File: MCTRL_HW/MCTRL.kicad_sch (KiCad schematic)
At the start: 22 parts, among them Q1 NMOS, Q2 NMOS, Q3 NMOS, Q4 NMOS, U1 IR2110, U2 IR2110

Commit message: more changes
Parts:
- removed Q1, Q2, Q3, Q4: NMOS, symbol Simulation_SPICE:NMOS
- added J1, J2, J3: 393570004, MCTRL:393570004, symbol MCTRL:393570004
- added U3, U4, U5, U6: IPD70R360P7SAUMA1, MCTRL:IPD70R360P7SAUMA1, symbol MCTRL:IPD70R360P7SAUMA1
- D1, D4: footprint (none) -> Diode_THT:D_DO-15_P12.70mm_Horizontal
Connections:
- net +3.3V: now also J2.1
- net +VDD: now also J1.1, U3.2 (DRAIN), U5.2 (DRAIN)
- net at D6.2 (A), R4.2: now also U6.1 (GATE)
- net at D2.2 (A), R1.2: now also U3.1 (GATE)
- net at D3.2 (A), R2.2: now also U4.1 (GATE)
- net at D5.2 (A), R3.2: now also U5.1 (GATE)
- net +15V renamed +10V
- net +10V: now also J2.2
- net GD_D1: no longer names the net of U1.10 (HIN)
- net GD_D1: now also J3.1; no longer U2.12 (LIN)
- net GD_D2: no longer names the net of U1.12 (LIN)
- net GD_D2: now also J3.2; no longer U2.10 (HIN)
- removed net GND: C1.2, C2.2, C4.2, C6.2, U1.11 (SD), U1.13 (VSS), U1.2 (COM), U2.11 (SD), U2.13 (VSS), U2.2 (COM)
- net LOAD_L: no longer names the net of C3.2, U1.5 (VS)
- net LOAD_L: now also J1.2, U3.3 (SOURCE), U4.2 (DRAIN)
- net LOAD_N: no longer names the net of C5.2, U2.5 (VS)
- net LOAD_N: now also J1.3, U5.3 (SOURCE), U6.2 (DRAIN)
- new net: J3.3, U2.10 (HIN)
- new net: J3.4, U2.12 (LIN)
- new net: J2.3, U1.11 (SD), U2.11 (SD)
- new net COM: C2.2, C6.2, J1.4, U1.2 (COM), U2.2 (COM), U4.3 (SOURCE), U6.3 (SOURCE)
- new net VSS: C1.2, C4.2, J2.4, U1.13 (VSS), U2.13 (VSS)
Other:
- moved on the sheet: C1, C2, C3, C4, C5, C6, D1, D2, D3, D4, D5, D6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

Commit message: Unfinished PCB
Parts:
- removed U3, U4, U5, U6: IPD70R360P7SAUMA1, MCTRL:IPD70R360P7SAUMA1, symbol MCTRL:IPD70R360P7SAUMA1
- added U3, U4, U5, U6: IPAN60R125PFD7SXKSA1, MCTRL:IPAN60R125PFD7SXKSA1, symbol MCTRL:IPAN60R125PFD7SXKSA1
- C1, C4: footprint Capacitor_THT:C_Disc_D5.0mm_W2.5mm_P5.00mm -> MCTRL:UUP1H0R1MCL1GS
- C2, C6: footprint (none) -> MCTRL:EEEFK1H220P
- C3, C5: footprint Capacitor_THT:C_Disc_D5.0mm_W2.5mm_P5.00mm -> MCTRL:UWP1HR22MCL1GB
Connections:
- net +10V: now also J2.1; no longer J2.2
- net +3.3V: now also J2.2; no longer J2.1
- net +VDD: now also U3.2 (DRAIN), U5.2 (DRAIN)
- net COM: now also U4.3 (SOURCE), U6.3 (SOURCE)
- net at J3.1: now also U2.12 (LIN); no longer U1.10 (HIN)
- net at J3.2: now also U2.10 (HIN); no longer U1.12 (LIN)
- net at J3.3: now also U1.10 (HIN); no longer U2.10 (HIN)
- net at J3.4: now also U1.12 (LIN); no longer U2.12 (LIN)
- net at C5.2, J1.3, U2.5 (VS): now also U5.3 (SOURCE), U6.2 (DRAIN)
- net at C3.2, J1.2, U1.5 (VS): now also U3.3 (SOURCE), U4.2 (DRAIN)
- net at D6.2 (A), R4.2: now also U6.1 (GATE)
- net at D3.1 (K), R2.1: now also U4.1 (GATE); no longer U1.1 (LO)
- net at D2.2 (A), R1.2: now also U3.1 (GATE)
- net at D3.2 (A), R2.2: now also U1.1 (LO)
- net at D5.2 (A), R3.2: now also U5.1 (GATE)
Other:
- moved on the sheet: J1, R2

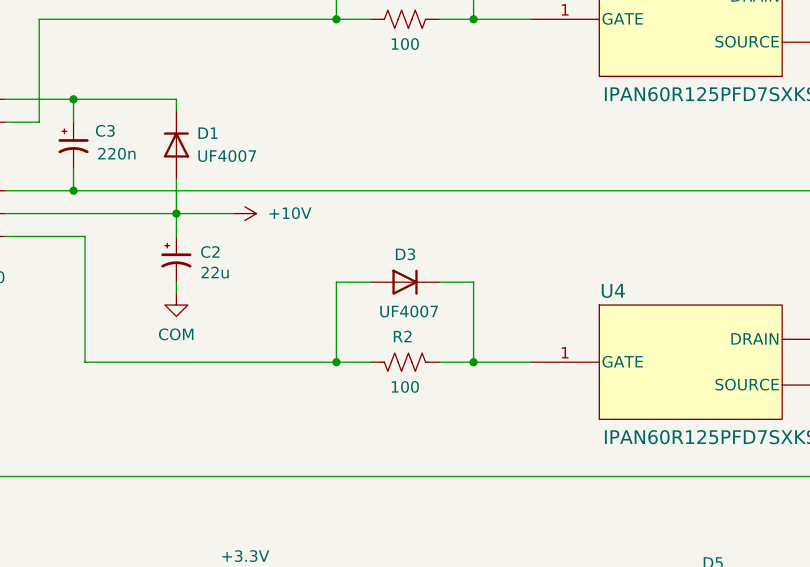
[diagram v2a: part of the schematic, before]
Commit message: Fixed diode direction
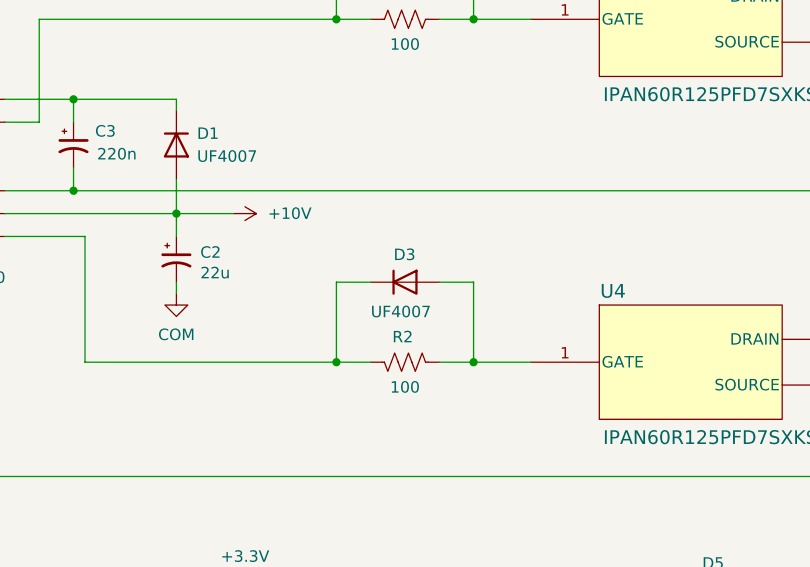
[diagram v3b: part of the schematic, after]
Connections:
- net at R2.1, U4.1 (GATE): now also D3.2 (A); no longer D3.1 (K)
- net at R2.2, U1.1 (LO): now also D3.1 (K); no longer D3.2 (A)
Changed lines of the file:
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@@
 		(lib_id "Device:D")
 		(at 137.16 62.23 0)
-		(mirror y)
 		(unit 1)
 		(body_style 1)
@@
 		(dnp no)
 		(property "Reference" "D3"
-			(at 138.43 59.182 0)
+			(at 135.89 59.182 0)
 			(show_name no)
 			(do_not_autoplace no)
@@
 		)
 		(property "Value" "UF4007"
-			(at 140.97 65.532 0)
+			(at 133.35 65.532 0)
 			(show_name no)
 			(do_not_autoplace no)
